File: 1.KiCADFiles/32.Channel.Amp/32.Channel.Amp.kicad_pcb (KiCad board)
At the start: 2 copper layers, 64 x 3 mm, 33 parts

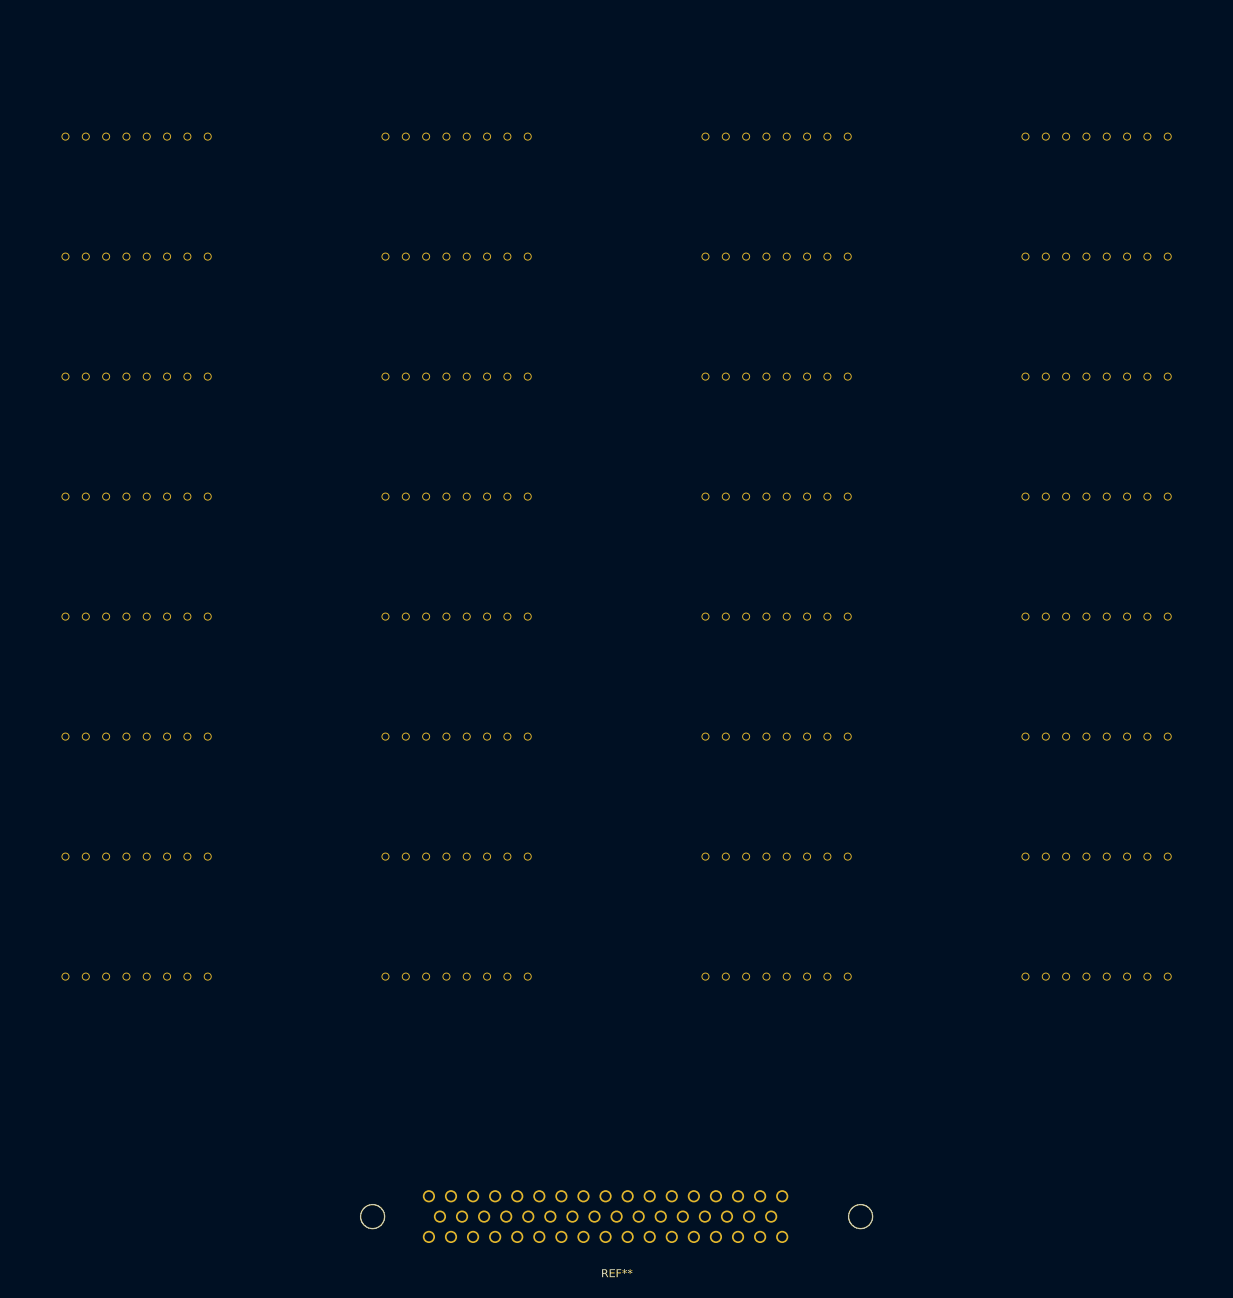
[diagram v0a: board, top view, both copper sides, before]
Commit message: Added DB9 and Created a General Layout
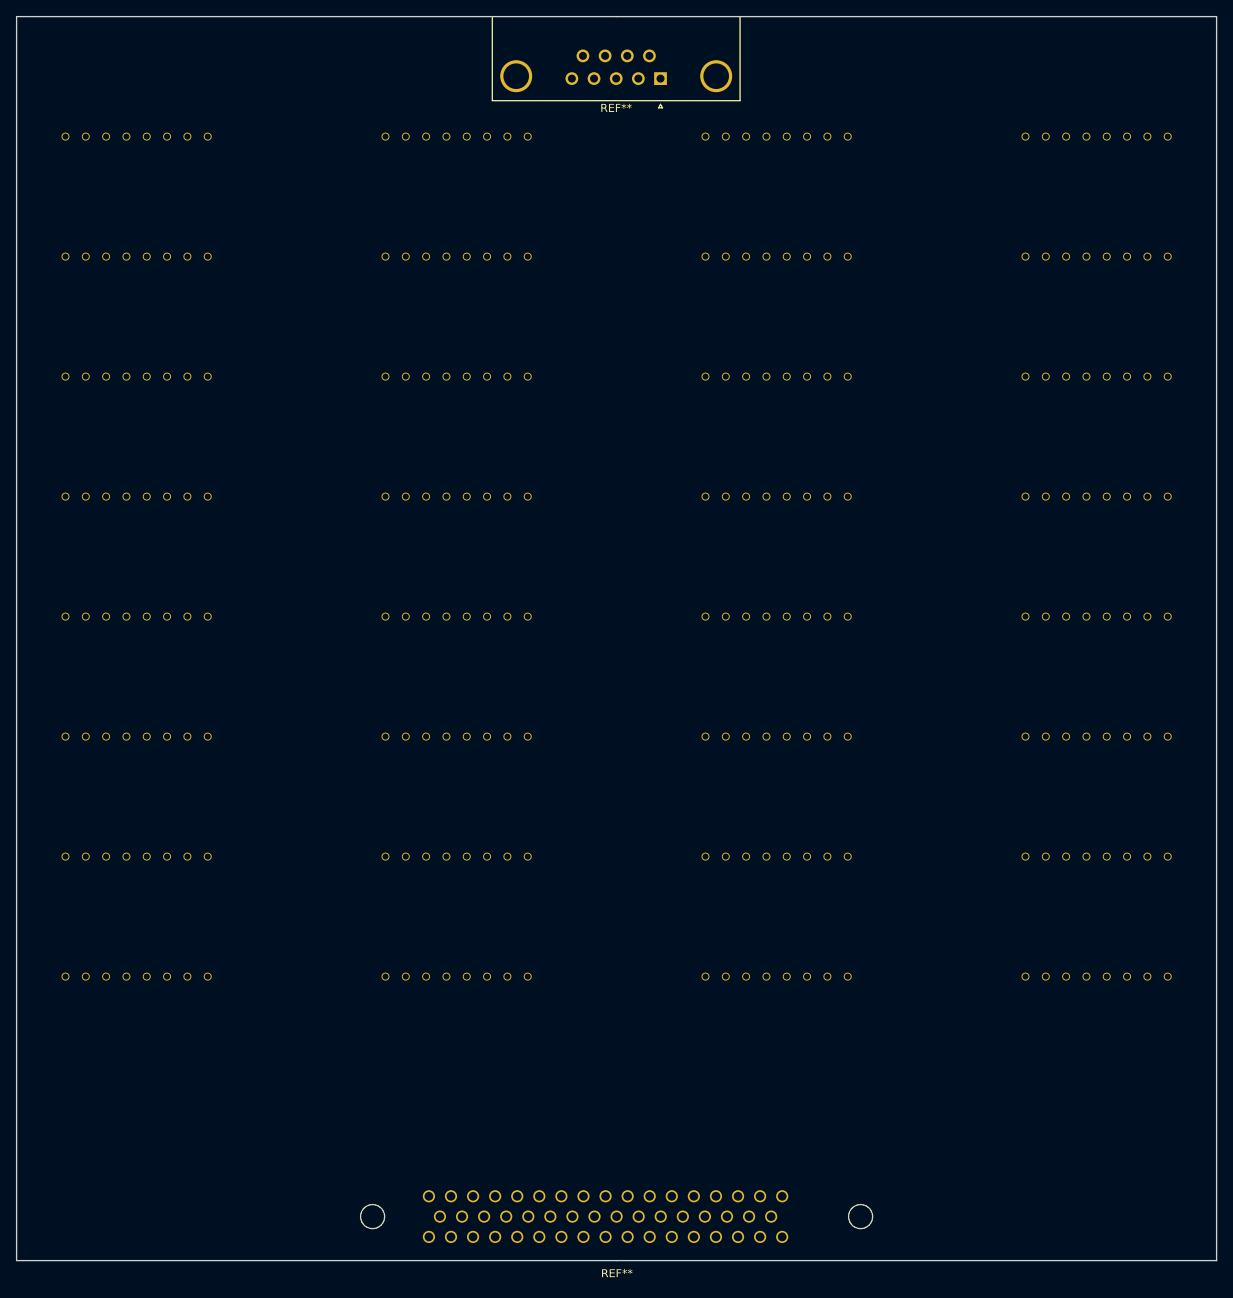
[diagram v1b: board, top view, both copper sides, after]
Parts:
- added REF**: DSUB-9_Male_Horizontal_P2.77x2.84mm_EdgePinOffset4.94mm_Hou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, Connector_Dsub:DSUB-9_Male_Horizontal_P2.77x2.84mm_EdgePinOffset4.94mm_Housed_MountingHolesOffset7.48mm, F.Cu at (110.5, 22.8)
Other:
- board size 64 x 3 mm -> 150 x 155.5 mm
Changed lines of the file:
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@@
     (pad "8" thru_hole circle (at 8.89 0) (size 1 1) (drill 0.762) (layers "*.Cu" "*.Mask"))
+  )
+  (footprint "Connector_Dsub:DSUB-9_Male_Horizontal_P2.77x2.84mm_EdgePinOffset4.94mm_Housed_MountingHolesOffset7.48mm" (layer "F.Cu")
+    (at 110.49 22.75 180)
+    (descr "9-pin D-Sub connector, horizontal/angled (90 deg), THT-mount, male, pitch 2.77x2.84mm, pin-PCB-offset 4.9399999999999995mm, distance of mounting holes 25mm, distance of mounting holes to PCB edge 7.4799999999999995mm, see https://disti-assets.s3.amazonaws.com/tonar/files/datasheets/16730.pdf")
+    (tags "9-pin D-Sub connector horizontal angled 90deg THT male pitch 2.77x2.84mm pin-PCB-offset 4.9399999999999995mm mounting-holes-distance 25mm mounting-hole-offset 25mm")
+    (attr through_hole)
+    (fp_text reference "REF**" (at 5.54 -3.7) (layer "F.SilkS")
+        (effects (font (size 1 1) (thickness 0.15)))
+    )
+    (fp_text value "DSUB-9_Male_Horizontal_P2.77x2.84mm_EdgePinOffset4.94mm_Housed_MountingHolesOffset7.48mm" (at 5.54 15.68) (layer "F.Fab")
+        (effects (font (size 1 1) (thickness 0.15)))
+    )
+    (fp_text user "${REFERENCE}" (at 5.54 11.18) (layer "F.Fab")
+        (effects (font (size 1 1) (thickness 0.15)))
+    )
+    (fp_line (start -9.945 -2.76) (end 21.025 -2.76)
+      (stroke (width 0.12) (type solid)) (layer "F.SilkS"))
+    (fp_line (start -9.945 7.72) (end -9.945 -2.76)
+      (stroke (width 0.12) (type solid)) (layer "F.SilkS"))
+    (fp_line (start -0.25 -3.654338) (end 0.25 -3.654338)
+      (stroke (width 0.12) (type solid)) (layer "F.SilkS"))
+    (fp_line (start 0 -3.221325) (end -0.25 -3.654338)
+      (stroke (width 0.12) (type solid)) (layer "F.SilkS"))
+    (fp_line (start 0.25 -3.654338) (end 0 -3.221325)
+      (stroke (width 0.12) (type solid)) (layer "F.SilkS"))
+    (fp_line (start 21.025 -2.76) (end 21.025 7.72)
+      (stroke (width 0.12) (type solid)) (layer "F.SilkS"))
+    (fp_line (start -10.4 -3.25) (end -10.4 14.7)
+      (stroke (width 0.05) (type solid)) (layer "F.CrtYd"))
+    (fp_line (start -10.4 14.7) (end 21.5 14.7)
+      (stroke (width 0.05) (type solid)) (layer "F.CrtYd"))
+    (fp_line (start 21.5 -3.25) (end -10.4 -3.25)
+      (stroke (width 0.05) (type solid)) (layer "F.CrtYd"))
+    (fp_line (start 21.5 14.7) (end 21.5 -3.25)
+      (stroke (width 0.05) (type solid)) (layer "F.CrtYd"))
+    (fp_line (start -9.885 -2.7) (end -9.885 7.78)
+      (stroke (width 0.1) (type solid)) (layer "F.Fab"))
+    (fp_line (start -9.885 7.78) (end -9.885 8.18)
+      (stroke (width 0.1) (type solid)) (layer "F.Fab"))
+    (fp_line (start -9.885 7.78) (end 20.965 7.78)
+      (stroke (width 0.1) (type solid)) (layer "F.Fab"))
+    (fp_line (start -9.885 8.18) (end 20.965 8.18)
+      (stroke (width 0.1) (type solid)) (layer "F.Fab"))
+    (fp_line (start -9.46 8.18) (end -9.46 13.18)
+      (stroke (width 0.1) (type solid)) (layer "F.Fab"))
+    (fp_line (start -9.46 13.18) (end -4.46 13.18)
+      (stroke (width 0.1) (type solid)) (layer "F.Fab"))
+    (fp_line (start -8.56 7.78) (end -8.56 0.3)
+      (stroke (width 0.1) (type solid)) (layer "F.Fab"))
+    (fp_line (start -5.36 7.78) (end -5.36 0.3)
+      (stroke (width 0.1) (type solid)) (layer "F.Fab"))
+    (fp_line (start -4.46 8.18) (end -9.46 8.18)
+      (stroke (width 0.1) (type solid)) (layer "F.Fab"))
+    (fp_line (start -4.46 13.18) (end -4.46 8.18)
+      (stroke (width 0.1) (type solid)) (layer "F.Fab"))
+    (fp_line (start -2.61 8.18) (end -2.61 14.18)
+      (stroke (width 0.1) (type solid)) (layer "F.Fab"))
+    (fp_line (start -2.61 14.18) (end 13.69 14.18)
+      (stroke (width 0.1) (type solid)) (layer "F.Fab"))
+    (fp_line (start 13.69 8.18) (end -2.61 8.18)
+      (stroke (width 0.1) (type solid)) (layer "F.Fab"))
+    (fp_line (start 13.69 14.18) (end 13.69 8.18)
+      (stroke (width 0.1) (type solid)) (layer "F.Fab"))
+    (fp_line (start 15.54 8.18) (end 15.54 13.18)
+      (stroke (width 0.1) (type solid)) (layer "F.Fab"))
+    (fp_line (start 15.54 13.18) (end 20.54 13.18)
+      (stroke (width 0.1) (type solid)) (layer "F.Fab"))
+    (fp_line (start 16.44 7.78) (end 16.44 0.3)
+      (stroke (width 0.1) (type solid)) (layer "F.Fab"))
+    (fp_line (start 19.64 7.78) (end 19.64 0.3)
+      (stroke (width 0.1) (type solid)) (layer "F.Fab"))
+    (fp_line (start 20.54 8.18) (end 15.54 8.18)
+      (stroke (width 0.1) (type solid)) (layer "F.Fab"))
+    (fp_line (start 20.54 13.18) (end 20.54 8.18)
+      (stroke (width 0.1) (type solid)) (layer "F.Fab"))
+    (fp_line (start 20.965 -2.7) (end -9.885 -2.7)
+      (stroke (width 0.1) (type solid)) (layer "F.Fab"))
+    (fp_line (start 20.965 7.78) (end -9.885 7.78)
+      (stroke (width 0.1) (type solid)) (layer "F.Fab"))
+    (fp_line (start 20.965 7.78) (end 20.965 -2.7)
+      (stroke (width 0.1) (type solid)) (layer "F.Fab"))
+    (fp_line (start 20.965 8.18) (end 20.965 7.78)
+      (stroke (width 0.1) (type solid)) (layer "F.Fab"))
+    (fp_arc (start -8.56 0.3) (mid -6.96 -1.3) (end -5.36 0.3)
+      (stroke (width 0.1) (type solid)) (layer "F.Fab"))
+    (fp_arc (start 16.44 0.3) (mid 18.04 -1.3) (end 19.64 0.3)
+      (stroke (width 0.1) (type solid)) (layer "F.Fab"))
+    (pad "0" thru_hole circle (at -6.96 0.3 180) (size 4 4) (drill 3.2) (layers "*.Cu" "*.Mask"))
+    (pad "0" thru_hole circle (at 18.04 0.3 180) (size 4 4) (drill 3.2) (layers "*.Cu" "*.Mask"))
+    (pad "1" thru_hole rect (at 0 0 180) (size 1.6 1.6) (drill 1) (layers "*.Cu" "*.Mask"))
+    (pad "2" thru_hole circle (at 2.77 0 180) (size 1.6 1.6) (drill 1) (layers "*.Cu" "*.Mask"))
+    (pad "3" thru_hole circle (at 5.54 0 180) (size 1.6 1.6) (drill 1) (layers "*.Cu" "*.Mask"))
+    (pad "4" thru_hole circle (at 8.31 0 180) (size 1.6 1.6) (drill 1) (layers "*.Cu" "*.Mask"))
+    (pad "5" thru_hole circle (at 11.08 0 180) (size 1.6 1.6) (drill 1) (layers "*.Cu" "*.Mask"))
+    (pad "6" thru_hole circle (at 1.385 2.84 180) (size 1.6 1.6) (drill 1) (layers "*.Cu" "*.Mask"))
+    (pad "7" thru_hole circle (at 4.155 2.84 180) (size 1.6 1.6) (drill 1) (layers "*.Cu" "*.Mask"))
+    (pad "8" thru_hole circle (at 6.925 2.84 180) (size 1.6 1.6) (drill 1) (layers "*.Cu" "*.Mask"))
+    (pad "9" thru_hole circle (at 9.695 2.84 180) (size 1.6 1.6) (drill 1) (layers "*.Cu" "*.Mask"))
+    (model "${KICAD6_3DMODEL_DIR}/Connector_Dsub.3dshapes/DSUB-9_Male_Horizontal_P2.77x2.84mm_EdgePinOffset4.94mm_Housed_MountingHolesOffset7.48mm.wrl"
+      (offset (xyz 0 0 0))
+      (scale (xyz 1 1 1))
+      (rotate (xyz 0 0 0))
+    )
   )
   (footprint "1.Local.Library:SMC-1-08-1-GT" (layer "F.Cu")
@@
     (pad "8" thru_hole circle (at 8.89 0) (size 1 1) (drill 0.762) (layers "*.Cu" "*.Mask"))
   )
+  (gr_line (start 105 15) (end 30 15)
+    (stroke (width 0.15) (type default)) (layer "Edge.Cuts"))
+  (gr_line (start 105 170.5) (end 30 170.5)
+    (stroke (width 0.15) (type default)) (layer "Edge.Cuts"))
+  (gr_line (start 105 170.5) (end 180 170.5)
+    (stroke (width 0.15) (type default)) (layer "Edge.Cuts"))
+  (gr_line (start 180 15) (end 180 170.5)
+    (stroke (width 0.15) (type default)) (layer "Edge.Cuts"))
+  (gr_line (start 105 15) (end 180 15)
+    (stroke (width 0.15) (type default)) (layer "Edge.Cuts"))
+  (gr_line (start 30 170.5) (end 30 15)
+    (stroke (width 0.15) (type default)) (layer "Edge.Cuts"))
+  (gr_line (start 105 90) (end 180 90)
+    (stroke (width 0.15) (type default)) (layer "User.8"))
+  (gr_line (start 105 165) (end 105 15)
+    (stroke (width 0.15) (type default)) (layer "User.8"))
+  (gr_line (start 105 90) (end 30 90)
+    (stroke (width 0.15) (type default)) (layer "User.8"))
+  (gr_line (start 105 165) (end 105 170.5)
+    (stroke (width 0.15) (type default)) (layer "User.8"))
 )

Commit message: Updated Files
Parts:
- added REF**: DSUB-9_Male_Horizontal_P2.77x2.84mm_EdgePinOffset4.94mm_Hou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, Connector_Dsub:DSUB-9_Male_Horizontal_P2.77x2.84mm_EdgePinOffset4.94mm_Housed_MountingHolesOffset7.48mm, F.Cu at (152.0, 7.70)
- moved REF** 42.5 mm to (70.7, 7.75)
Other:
- board size 150 x 155.5 mm -> 150 x 170.5 mm
